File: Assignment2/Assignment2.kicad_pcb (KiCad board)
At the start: 2 copper layers, 36 parts, among them J1 Conn_01x03, J3 USB_C_Receptacle_USB2.0_14P, J4 Conn_01x02, J5 Screw_Terminal_01x02, U1 RP2040, U2 W25Q128JVS, U3 NCP1117-3.3_SOT223, U4 BMP280, U5 BMI160, Y1 Crystal_GND24_Small

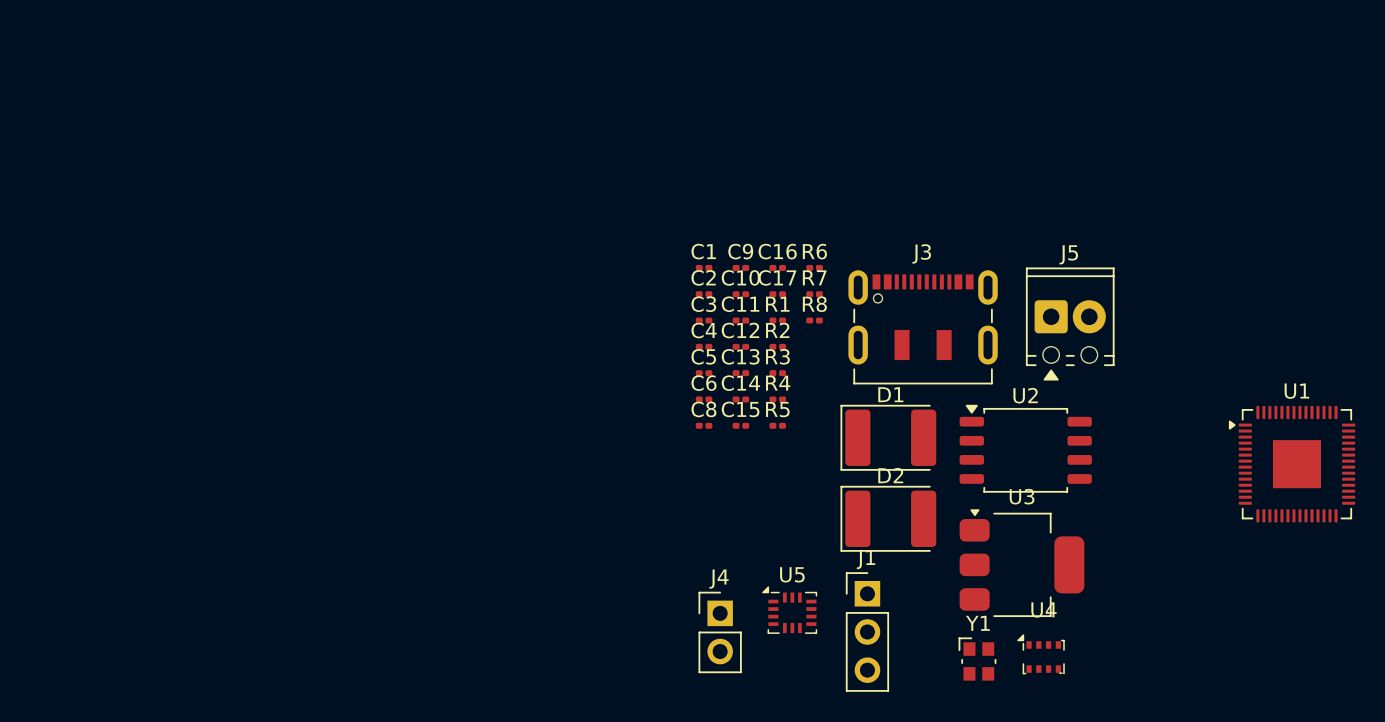
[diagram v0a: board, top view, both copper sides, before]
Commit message: Arrange PCB elements systematically. Drawing traces still left.
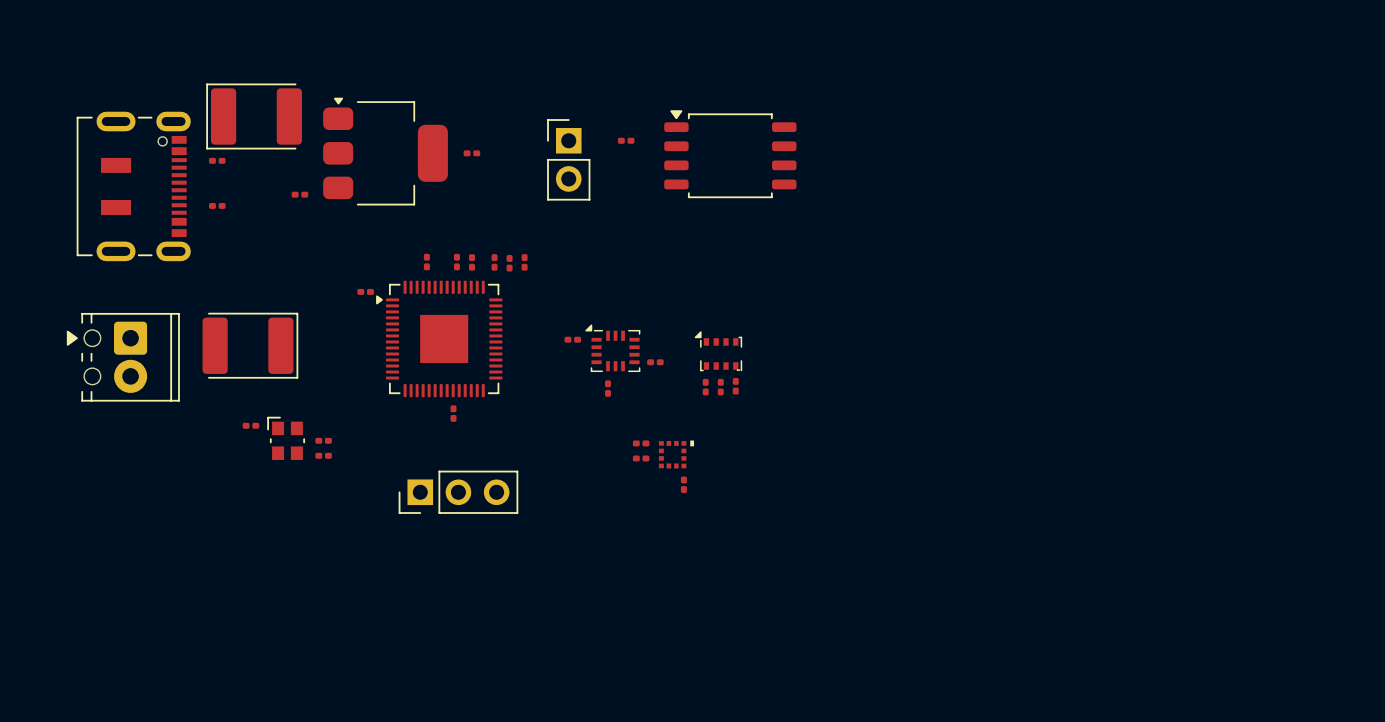
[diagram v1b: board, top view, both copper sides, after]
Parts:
- added R9: 1k, Resistor_SMD:R_0201_0603Metric, F.Cu at (111.8, 94.8)
- added U6: KX134-1211, Audio_Module:LGA12_2X2X0P9_ROM, F.Cu at (135.0, 95.8)
- moved J5 61.3 mm to (98.9, 88.0), turned to -90 degrees
- moved U1 57.3 mm to (119.8, 88.0)
- moved J3 53.4 mm to (99.1, 77.9), turned to -90 degrees
- moved U3 50.4 mm to (115.9, 75.7)
- moved D2 50.0 mm to (107.3, 73.2)
- moved Y1 48.3 mm to (109.4, 94.8)
- moved D1 43.2 mm to (106.8, 88.5), turned to 180 degrees
- moved R4 40.5 mm to (104.7, 76.2)
- moved R3 38.9 mm to (104.7, 79.2)
- moved C10 33.7 mm to (106.9, 93.8), turned to 180 degrees
- moved J4 33.0 mm to (128.1, 74.9)
- moved C12 31.0 mm to (110.2, 78.5)
- moved J1 30.5 mm to (118.2, 98.2), turned to 90 degrees
- moved U4 29.4 mm to (138.2, 89.0)
- moved C13 28.3 mm to (111.8, 95.8)
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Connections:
- C13 pad 1: /XOUT -> Net-(C13-Pad1)
- U1 pad 26: unconnected-(U1-RUN-Pad26) -> +3V3
- Y1 pad 3: /XOUT -> Net-(C13-Pad1)

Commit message: Join traces. USB Differential Pair still left.
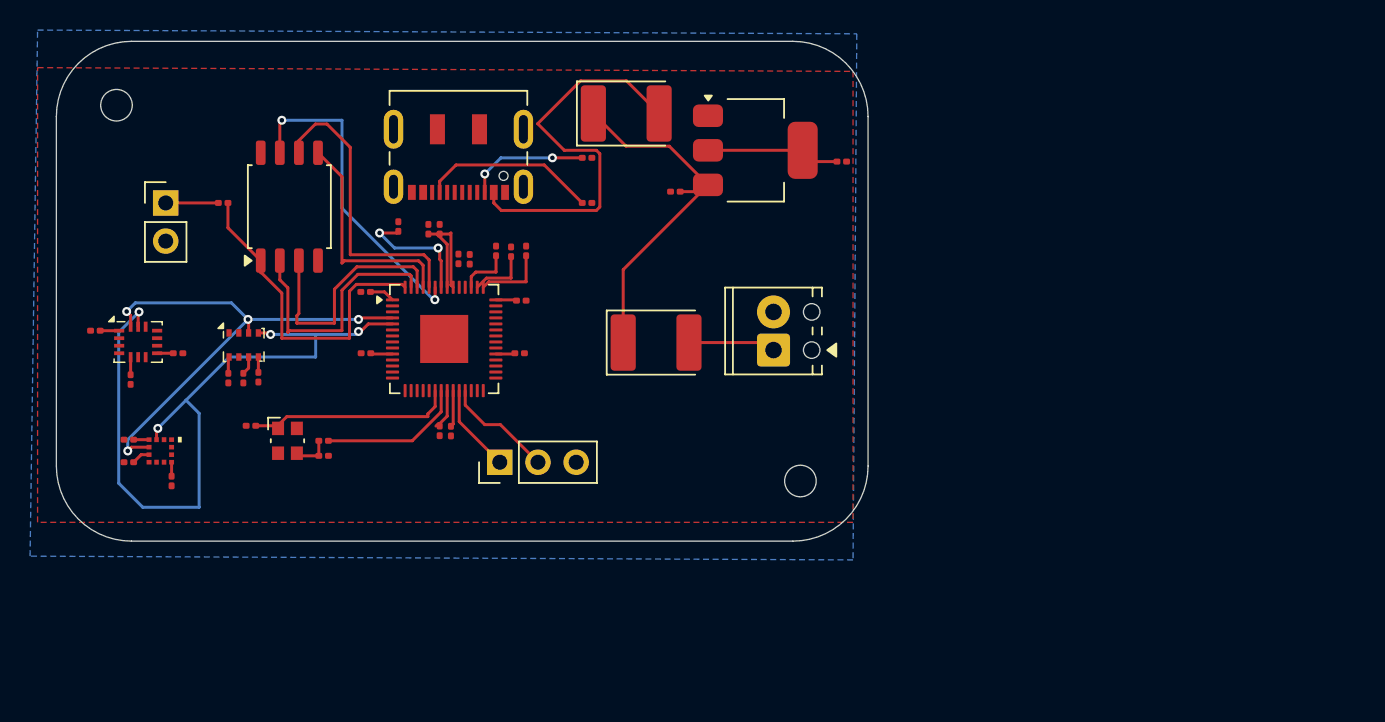
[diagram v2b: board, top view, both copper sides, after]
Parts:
- added C18: 100n, Capacitor_SMD:C_0201_0603Metric, F.Cu at (116.8, 80.6)
- added C19: 100n, Capacitor_SMD:C_0201_0603Metric, F.Cu at (119.5, 94.2)
- added C20: 100n, Capacitor_SMD:C_0201_0603Metric, F.Cu at (114.6, 89.0)
- added C21: 100n, Capacitor_SMD:C_0201_0603Metric, F.Cu at (124.8, 89.0)
- added C22: 100n, Capacitor_SMD:C_0201_0603Metric, F.Cu at (119.5, 80.8)
- added C7: 100n, Capacitor_SMD:C_0201_0603Metric, F.Cu at (124.9, 85.5)
- added REF**: MountingHole_2.1mm, MountingHole:MountingHole_2.1mm, F.Cu at (98.0, 72.5)
- added REF**: MountingHole_2.1mm, MountingHole:MountingHole_2.1mm, F.Cu at (143.5, 97.5)
- moved J5 42.8 mm to (141.7, 88.8), turned to 90 degrees
- moved C12 36.1 mm to (146.2, 76.2)
- moved R8 34.1 mm to (98.8, 94.8)
- moved C1 34.1 mm to (101.7, 97.5)
- moved U6 34.1 mm to (100.9, 95.5)
- moved C17 34.1 mm to (98.8, 96.2)
- moved C14 31.8 mm to (106.4, 90.7)
- moved C15 31.8 mm to (105.4, 90.7)
- moved C16 31.8 mm to (98.9, 90.8)
- moved C9 31.8 mm to (102.1, 89.0)
- moved R6 31.8 mm to (107.4, 90.6)
- moved R7 31.8 mm to (96.6, 87.5)
- moved U4 31.8 mm to (106.5, 88.5)
- moved U5 31.8 mm to (99.4, 88.2)
- moved U2 29.5 mm to (109.5, 79.2), turned to 90 degrees
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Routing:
- net /GPIO3: track 0.00 -> 50.5 mm, vias 0 -> 4
- net +3V3: track 0.00 -> 41.8 mm
- net /GPIO2: track 0.00 -> 34.3 mm, vias 0 -> 4
- net Net-(D2-A): track 0.00 -> 26.7 mm
- net VBUS: track 0.00 -> 24.5 mm
- net /QSPI_SS: track 0.00 -> 22.9 mm
- net /QSPI_SD3: track 0.00 -> 21.6 mm, vias 0 -> 2
- net /QSPI_SCLK: track 0.00 -> 19.7 mm
- net /QSPI_SD1: track 0.00 -> 17.2 mm
- net /QSPI_SD2: track 0.00 -> 16.3 mm
- net /QSPI_SD0: track 0.00 -> 15.0 mm
- net +1V1: track 0.00 -> 14.3 mm, vias 0 -> 2
- net /XIN: track 0.00 -> 13.9 mm
- net Net-(J3-CC2): track 0.00 -> 11.7 mm
- net /XOUT: track 0.00 -> 9.71 mm
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- added copper zone on B.Cu, net +3V3
- added copper zone on F.Cu, net GND
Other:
- board outline added: 54 x 33.2 mm
